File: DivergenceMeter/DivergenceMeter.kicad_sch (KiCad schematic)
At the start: 19 parts, among them U1 SN74141N

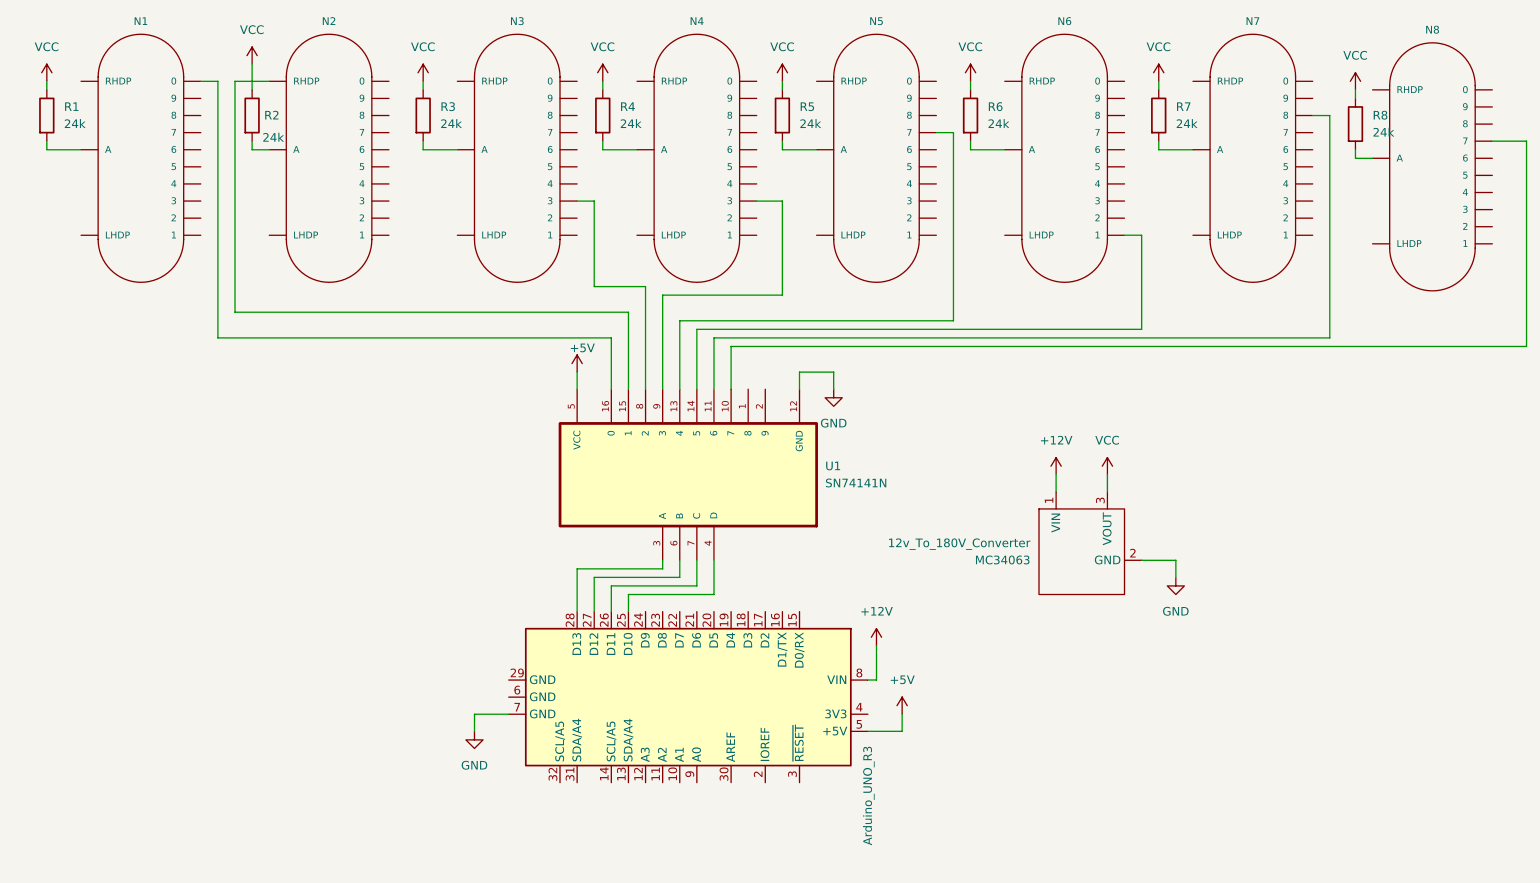
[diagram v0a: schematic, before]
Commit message: Update schematic, BOM and add 3d models
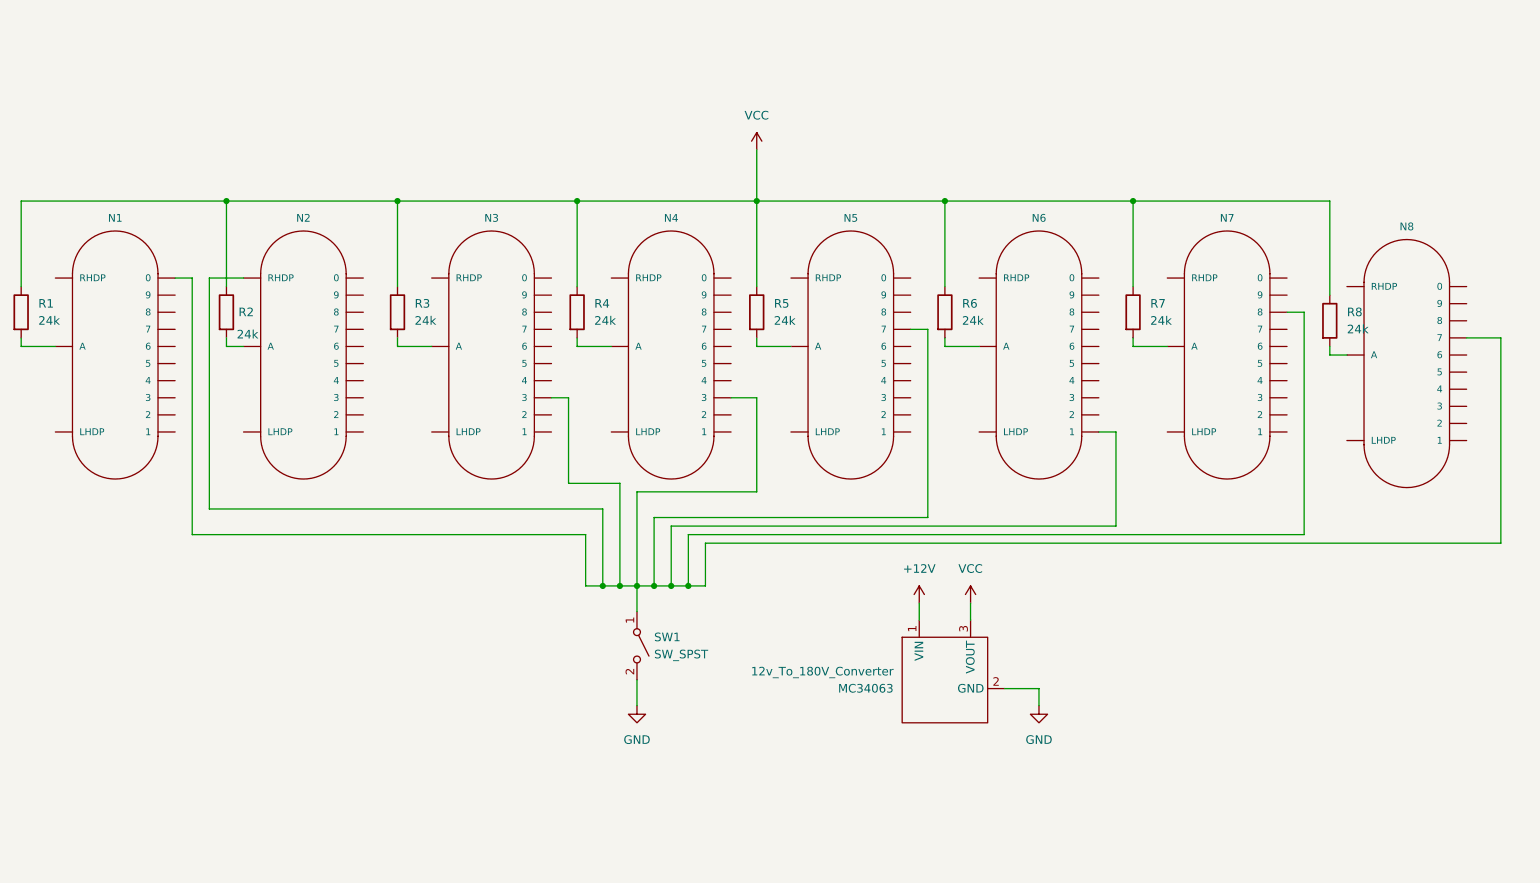
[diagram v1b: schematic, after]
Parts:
- removed A1: Arduino_UNO_R3, Module:Arduino_UNO_R3, symbol MCU_Module:Arduino_UNO_R3
- removed U1: SN74141N, SN74141N:DIP762W46P254L2134H508Q16, symbol SN74141N:SN74141N
- added SW1: SW_SPST, symbol Switch:SW_SPST
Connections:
- net GND: now also SW1.2 (B)
- net at N3.3: now also N1.0, N2.RHDP, N4.3, N5.7, N6.1, N7.8, N8.7, SW1.1 (A)
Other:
- moved on the sheet: 12v_To_180V_Converter, N1, N2, N3, N4, N5, N6, N7, N8, R1, R2, R3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
